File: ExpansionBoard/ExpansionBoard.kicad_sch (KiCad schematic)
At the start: 11 parts, among them J2 Screw_Terminal_01x02, J3 Conn_02x19_Odd_Even, J4 Conn_02x19_Odd_Even

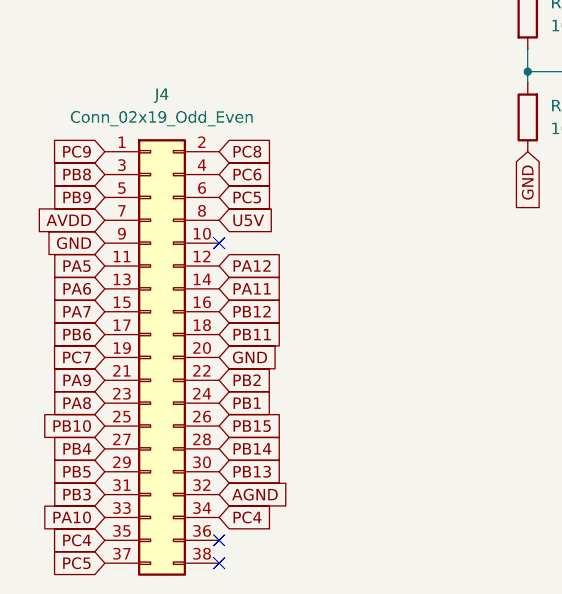
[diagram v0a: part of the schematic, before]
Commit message: Revision PCB e Intento ADCs
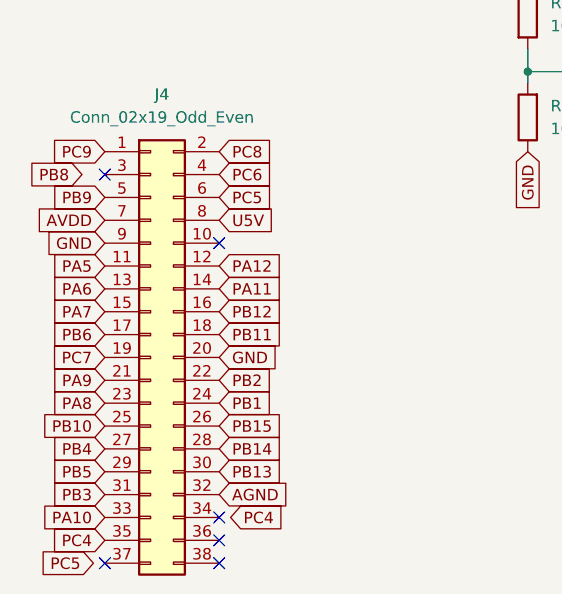
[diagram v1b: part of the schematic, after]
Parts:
- C1: footprint Capacitor_SMD:CP_Elec_3x5.3 -> Capacitor_SMD:C_1206_3216Metric
- R1, R2, R3, R4, R5, R6, R7: footprint Resistor_SMD:R_0603_1608Metric -> Resistor_SMD:R_1206_3216Metric
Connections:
- net PB8: no longer J4.3 (Pin_3)
- net PC4: no longer J4.34 (Pin_34)
- net PC5: no longer J4.37 (Pin_37)
- no-connect marks 7 -> 10
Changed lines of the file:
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@@
+	)
+	(no_connect
+		(at 29.21 92.71)
 	)
 	(no_connect
@@
 	)
 	(no_connect
+		(at 29.21 135.89)
+	)
+	(no_connect
 		(at 41.91 100.33)
 	)
 	(no_connect
 		(at 41.91 133.35)
+	)
+	(no_connect
+		(at 41.91 130.81)
 	)
 	(wire
@@
 	(global_label "PB8"
 		(shape input)
-		(at 29.21 92.71 180)
-		(fields_autoplaced yes)
-		(effects
-			(font
-				(size 1.27 1.27)
-			)
-			(justify right)
-		)
-		(property "Intersheetrefs" "${INTERSHEET_REFS}"
-			(at 22.4753 92.71 0)
+		(at 26.67 92.71 180)
+		(fields_autoplaced yes)
+		(effects
+			(font
+				(size 1.27 1.27)
+			)
+			(justify right)
+		)
+		(property "Intersheetrefs" "${INTERSHEET_REFS}"
+			(at 19.9353 92.71 0)
 			(effects
 				(font
@@
 	(global_label "PC4"
 		(shape input)
-		(at 41.91 130.81 0)
-		(fields_autoplaced yes)
-		(effects
-			(font
-				(size 1.27 1.27)
-			)
-			(justify left)
-		)
-		(property "Intersheetrefs" "${INTERSHEET_REFS}"
-			(at 48.6447 130.81 0)
+		(at 43.18 130.81 0)
+		(fields_autoplaced yes)
+		(effects
+			(font
+				(size 1.27 1.27)
+			)
+			(justify left)
+		)
+		(property "Intersheetrefs" "${INTERSHEET_REFS}"
+			(at 49.9147 130.81 0)
 			(effects
 				(font
@@
 	(global_label "PC5"
 		(shape input)
-		(at 29.21 135.89 180)
-		(fields_autoplaced yes)
-		(effects
-			(font
-				(size 1.27 1.27)
-			)
-			(justify right)
-		)
-		(property "Intersheetrefs" "${INTERSHEET_REFS}"
-			(at 22.4753 135.89 0)
+		(at 27.94 135.89 180)
+		(fields_autoplaced yes)
+		(effects
+			(font
+				(size 1.27 1.27)
+			)
+			(justify right)
+		)
+		(property "Intersheetrefs" "${INTERSHEET_REFS}"
+			(at 21.2053 135.89 0)
 			(effects
 				(font
@@
 			)
 		)
-		(property "Footprint" "Resistor_SMD:R_0603_1608Metric"
+		(property "Footprint" "Resistor_SMD:R_1206_3216Metric"
 			(at 106.68 32.258 90)
 			(effects
@@
 			)
 		)
-		(property "Footprint" "Capacitor_SMD:CP_Elec_3x5.3"
+		(property "Footprint" "Capacitor_SMD:C_1206_3216Metric"
 			(at 91.1352 90.17 0)
 			(effects
@@
 			)
 		)
-		(property "Footprint" "Resistor_SMD:R_0603_1608Metric"
+		(property "Footprint" "Resistor_SMD:R_1206_3216Metric"
 			(at 83.82 32.258 90)
 			(effects
@@
 			)
 		)
-		(property "Footprint" "Resistor_SMD:R_0603_1608Metric"
+		(property "Footprint" "Resistor_SMD:R_1206_3216Metric"
 			(at 106.68 43.688 90)
 			(effects
@@
 			)
 		)
-		(property "Footprint" "Resistor_SMD:R_0603_1608Metric"
+		(property "Footprint" "Resistor_SMD:R_1206_3216Metric"
 			(at 74.422 74.93 90)
 			(effects
@@
 			)
 		)
-		(property "Footprint" "Resistor_SMD:R_0603_1608Metric"
+		(property "Footprint" "Resistor_SMD:R_1206_3216Metric"
 			(at 77.978 86.36 90)
 			(effects
@@
 			)
 		)
-		(property "Footprint" "Resistor_SMD:R_0603_1608Metric"
+		(property "Footprint" "Resistor_SMD:R_1206_3216Metric"
 			(at 83.82 43.688 90)
 			(effects
@@
 			)
 		)
-		(property "Footprint" "Resistor_SMD:R_0603_1608Metric"
+		(property "Footprint" "Resistor_SMD:R_1206_3216Metric"
 			(at 129.54 37.338 90)
 			(effects

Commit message: TFG Finalizado V1
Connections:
- net PB1 is gone; now on net PA6: J4.24 (Pin_24), R2.2
- net PB11 is gone; now on net PA0: J4.18 (Pin_18), R1.1
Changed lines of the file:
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@@
+	)
+	(junction
+		(at 114.3 30.48)
+		(diameter 0)
+		(color 0 0 0 0)
+	)
+	(junction
+		(at 77.47 30.48)
+		(diameter 0)
+		(color 0 0 0 0)
 	)
 	(junction
@@
 	(wire
 		(pts
+			(xy 80.01 24.13) (xy 80.01 27.94)
+		)
+		(stroke
+			(width 0)
+			(type default)
+		)
+	)
+	(wire
+		(pts
 			(xy 76.2 81.28) (xy 76.2 82.55)
 		)
@@
 	(wire
 		(pts
+			(xy 77.47 30.48) (xy 80.01 30.48)
+		)
+		(stroke
+			(width 0)
+			(type default)
+		)
+	)
+	(wire
+		(pts
 			(xy 95.25 30.48) (xy 102.87 30.48)
 		)
@@
 	(wire
 		(pts
+			(xy 116.84 30.48) (xy 114.3 30.48)
+		)
+		(stroke
+			(width 0)
+			(type default)
+		)
+	)
+	(wire
+		(pts
 			(xy 110.49 41.91) (xy 125.73 41.91)
 		)
@@
 	(wire
 		(pts
+			(xy 72.39 30.48) (xy 77.47 30.48)
+		)
+		(stroke
+			(width 0)
+			(type default)
+		)
+	)
+	(wire
+		(pts
 			(xy 95.25 41.91) (xy 95.25 46.99)
 		)
@@
 	(wire
 		(pts
+			(xy 114.3 27.94) (xy 114.3 30.48)
+		)
+		(stroke
+			(width 0)
+			(type default)
+		)
+	)
+	(wire
+		(pts
 			(xy 87.63 81.28) (xy 76.2 81.28)
 		)
@@
 	(wire
 		(pts
+			(xy 111.76 24.13) (xy 111.76 27.94)
+		)
+		(stroke
+			(width 0)
+			(type default)
+		)
+	)
+	(wire
+		(pts
+			(xy 114.3 30.48) (xy 110.49 30.48)
+		)
+		(stroke
+			(width 0)
+			(type default)
+		)
+	)
+	(wire
+		(pts
 			(xy 95.25 24.13) (xy 95.25 30.48)
 		)
@@
 	(wire
 		(pts
+			(xy 77.47 27.94) (xy 77.47 30.48)
+		)
+		(stroke
+			(width 0)
+			(type default)
+		)
+	)
+	(wire
+		(pts
 			(xy 87.63 41.91) (xy 95.25 41.91)
 		)
@@
 	(wire
 		(pts
+			(xy 111.76 27.94) (xy 114.3 27.94)
+		)
+		(stroke
+			(width 0)
+			(type default)
+		)
+	)
+	(wire
+		(pts
 			(xy 140.97 27.94) (xy 140.97 35.56)
 		)
@@
 	(wire
 		(pts
+			(xy 80.01 27.94) (xy 77.47 27.94)
+		)
+		(stroke
+			(width 0)
+			(type default)
+		)
+	)
+	(wire
+		(pts
 			(xy 87.63 77.47) (xy 87.63 81.28)
 		)
@@
 	(global_label "PB11"
 		(shape input)
-		(at 80.01 30.48 180)
-		(fields_autoplaced yes)
-		(effects
-			(font
-				(size 1.27 1.27)
-			)
-			(justify right)
-		)
-		(property "Intersheetrefs" "${INTERSHEET_REFS}"
-			(at 72.0658 30.48 0)
+		(at 72.39 30.48 180)
+		(fields_autoplaced yes)
+		(effects
+			(font
+				(size 1.27 1.27)
+			)
+			(justify right)
+		)
+		(property "Intersheetrefs" "${INTERSHEET_REFS}"
+			(at 64.4458 30.48 0)
 			(effects
 				(font
@@
 		)
 	)
+	(global_label "PA6"
+		(shape input)
+		(at 111.76 24.13 90)
+		(fields_autoplaced yes)
+		(effects
+			(font
+				(size 1.27 1.27)
+			)
+			(justify left)
+		)
+		(property "Intersheetrefs" "${INTERSHEET_REFS}"
+			(at 111.76 17.5767 90)
+			(effects
+				(font
+					(size 1.27 1.27)
+				)
+				(justify left)
+				(hide yes)
+			)
+		)
+	)
 	(global_label "5V"
 		(shape input)
@@
 		)
 	)
+	(global_label "PA0"
+		(shape input)
+		(at 80.01 24.13 90)
+		(fields_autoplaced yes)
+		(effects
+			(font
+				(size 1.27 1.27)
+			)
+			(justify left)
+		)
+		(property "Intersheetrefs" "${INTERSHEET_REFS}"
+			(at 80.01 17.5767 90)
+			(effects
+				(font
+					(size 1.27 1.27)
+				)
+				(justify left)
+				(hide yes)
+			)
+		)
+	)
 	(global_label "PC6"
 		(shape input)
@@
 	(global_label "PB1"
 		(shape input)
-		(at 110.49 30.48 0)
-		(fields_autoplaced yes)
-		(effects
-			(font
-				(size 1.27 1.27)
-			)
-			(justify left)
-		)
-		(property "Intersheetrefs" "${INTERSHEET_REFS}"
-			(at 117.2247 30.48 0)
-			(effects
-				(font
+		(at 116.84 30.48 0)
+		(fields_autoplaced yes)
+		(effects
+			(font
+				(size 1.27 1.27)
+			)
+			(justify left)
+		)
+		(property "Intersheetrefs" "${INTERSHEET_REFS}"
+			(at 123.5747 30.48 0)
+			(effects
+				(font
